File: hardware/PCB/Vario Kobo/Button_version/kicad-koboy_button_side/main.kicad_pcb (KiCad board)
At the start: 2 copper layers, 78.1 x 17.1 mm, 24 parts

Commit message: Restructure Vario Kobo schematic into main + power supply sheets
- Rename the KiCad project to main (main.kicad_pro/.kicad_sch/.kicad_pcb)
  and drop the empty "Alimentation" top-level sheet left by the Eagle import.
- Move the ADP160 regulator (R3, C1, C2) into a "Power supply" sub-sheet.
- Redraw the main sheet on A3 by function (barometer, Kobo connector + GPS,
  programming/MCLR, button, MAS6240 audio) with net labels instead of long
  wires, and add design notes per block.
- Add no-connect flags and PWR_FLAGs: ERC goes from 20 violations to
  11 warnings (Eagle pin types), no errors.
- Update the PCB from the schematic (renamed nets, same routing).
- README: refresh the ERC/DRC open issues and the project path.

Netlist topology, values and footprints are unchanged.

Co-Authored-By: Claude Opus 5.5 <noreply@anthropic.com>
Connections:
- net AUDIO_OUT renamed /AUDIO_OUT
- net BATT+ renamed /BATT+
- net BUZZER_A renamed /BUZZER_A
- net BUZZER_B renamed /BUZZER_B
- net KOBO_EN renamed /KOBO_EN
- net KOBO_RX renamed /KOBO_RX
- net Net-(MAS0-EN1) renamed /MAS_EN1
- net Net-(MAS0-EN2) renamed /MAS_EN2
- net Net-(MS5611-SCL) renamed /SCL
- net Net-(MS5611-SDI/SDA) renamed /SDA
- net Net-(PIC0-*MCLR/VPP/RA5) renamed /MCLR
- net Net-(PIC0-PGC1/AN3/C1INC/C2INA/U2RX/U2BCLK/CN5/RB1) renamed /PGC1
- net PA6H_RX renamed /PA6H_RX
- net PA6H_TX renamed /PA6H_TX
- net PROUT renamed /PROUT
- net SWITCH renamed /SWITCH

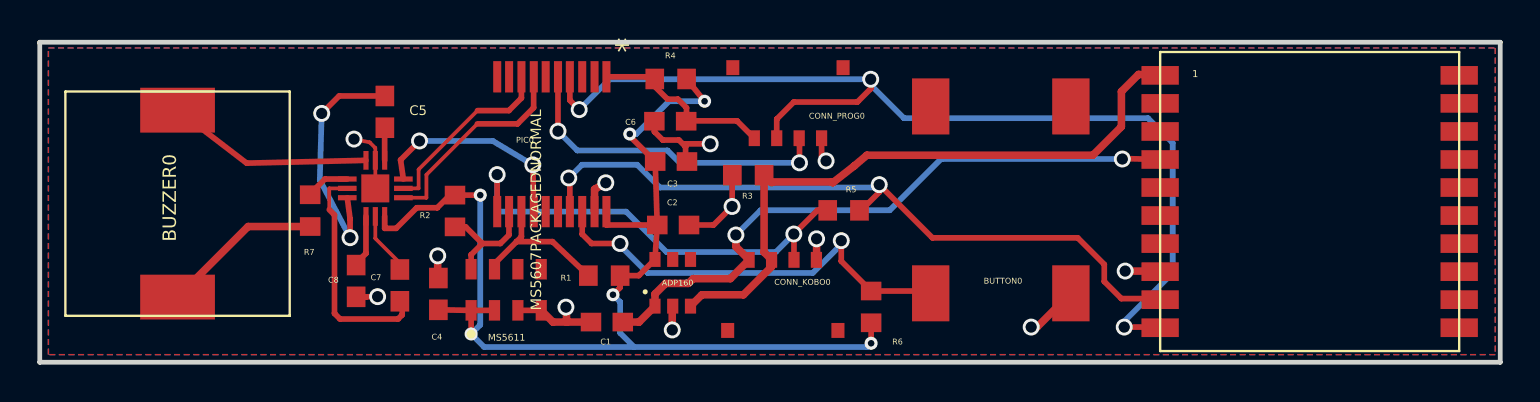
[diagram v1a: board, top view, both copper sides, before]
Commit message: Rename references and lay out a readable silkscreen
- Rename the Eagle-style references to short standard ones:
  PIC0->U1, MS5611->U2, MAS0->U3, ADP160->U4, PA6H0->U5,
  CONN_KOBO0->J1, CONN_PROG0->J2, BUTTON0->SW1, BUZZER0->BZ1.
- Move every footprint reference field next to its part, 0.8 mm text,
  clear of pads, vias and the board edge, closer to its own part than
  to any other one.
- Add footprint-owned silkscreen texts: J1/J2 pin names and a "1" next
  to pin 1 of U1-U5, so they follow the parts if they move.
- Hide value fields; drop the Eagle "1" next to the GPS and move the U1
  "*" mark to F.Fab.
- README: DRC is down from 74 to 22 warnings (footprint outlines over pads).

Co-Authored-By: Claude Opus 5.5 <noreply@anthropic.com>
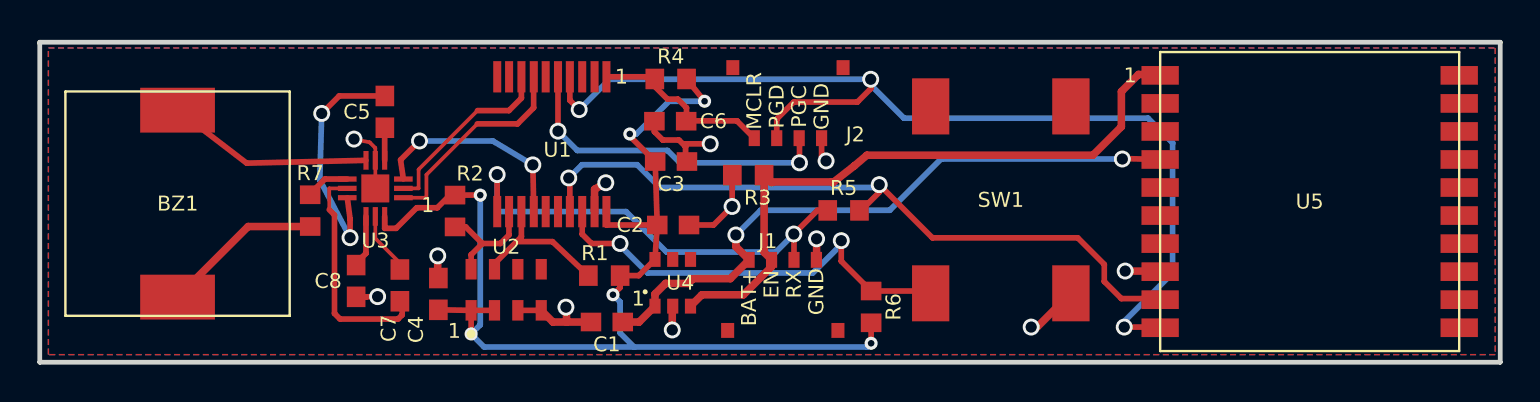
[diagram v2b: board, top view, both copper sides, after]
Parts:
- renumbered BUZZER0 to BZ1, CONN_KOBO0 to J1, CONN_PROG0 to J2, BUTTON0 to SW1, PIC0 to U1, MS5611 to U2, MAS0 to U3, ADP160 to U4, PA6H0 to U5
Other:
- board text removed: "1"

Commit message: Use Gekkio's FGPMMOPA6H for the GPS and clean up ERC
- U5 (GPS): replace the Eagle PA6H symbol and footprint with Gekkio's
  FGPMMOPA6H (gekkio-kicad-libs, CC BY 4.0, copied into libs/gekkio/ and
  registered in the project library tables). Same pad geometry; adds the
  datasheet's 1.2 mm NPTH under the module, a courtyard and a silkscreen
  outline clear of the pads. Unused pins flagged no-connect (datasheet:
  leave floating).
- Fix pin electrical types in the Eagle-imported symbols (connectors and
  switch passive, MAS6240/ADP160 power pins power in/out), add PWR_FLAGs
  on BATT+ and KOBO_EN, drop the now redundant one on PROUT.
- ERC: 0 errors, 0 warnings. DRC: 2 warnings (buzzer outline), no errors.
- README: refresh open issues, credit Gekkio. Ignore *.bak.

Co-Authored-By: Claude Opus 5.5 <noreply@anthropic.com>
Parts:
- U5: value PA6H -> FGPMMOPA6H; footprint Vario Kobo-import-fps:PA6H_PRINT -> Gekkio_RF_GPS:GlobalTop_FGPMMOPA6H

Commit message: Use KiCad's standard 0603 HandSolder footprints for R and C
Replace the Eagle-imported R0603/C0603 footprints of R1-R7 and C1-C8
with Resistor_SMD:R_0603_1608Metric_Pad0.98x0.95mm_HandSolder and
Capacitor_SMD:C_0603_1608Metric_Pad1.08x0.95mm_HandSolder, easier to
solder by hand. Footprint positions and routing are unchanged; the
track ends still land inside the new pads.

Reference fields are put back at their 0.8 mm silkscreen spots and all
Value fields are hidden on F.Fab (U2's moved off F.Silkscreen too).
Netlist topology unchanged, ERC 0, DRC 0 errors / 2 warnings (BZ1 outline).

Co-Authored-By: Claude Opus 5.5 <noreply@anthropic.com>
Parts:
- C1, C2, C3, C4, C5, C6, C7, C8: footprint Vario Kobo-import-fps:C0603 -> Capacitor_SMD:C_0603_1608Metric_Pad1.08x0.95mm_HandSolder
- R1, R2, R3, R4, R5, R6, R7: footprint Vario Kobo-import-fps:R0603 -> Resistor_SMD:R_0603_1608Metric_Pad0.98x0.95mm_HandSolder
